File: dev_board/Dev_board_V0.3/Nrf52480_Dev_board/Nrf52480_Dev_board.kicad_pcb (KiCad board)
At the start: 4 copper layers, 72 x 75 mm, 75 parts, among them J1 Conn_01x05, J10 Conn_01x02, J11 Conn_01x05, J12 Conn_01x02, J2 USB_B_Micro, J3 SWD Debug connector, J4 Conn_01x09, J5 Conn_02x07_Top_Bottom, J6 Conn_01x07, J7 Conn_01x02, SW1 SW_Push, SW2 SW_Push, SW3 SW_Push, SW4 SW_Push, SW5 SW_Push, U1 MDBT50Q-1MV2, U3 AP2112K-3.3, U4 LIS3MDL, U5 LSM6DSOXTR, U6 SST26VF080A-104I/SN, U7 DRV2605LDGS, Y1 32.768KHz

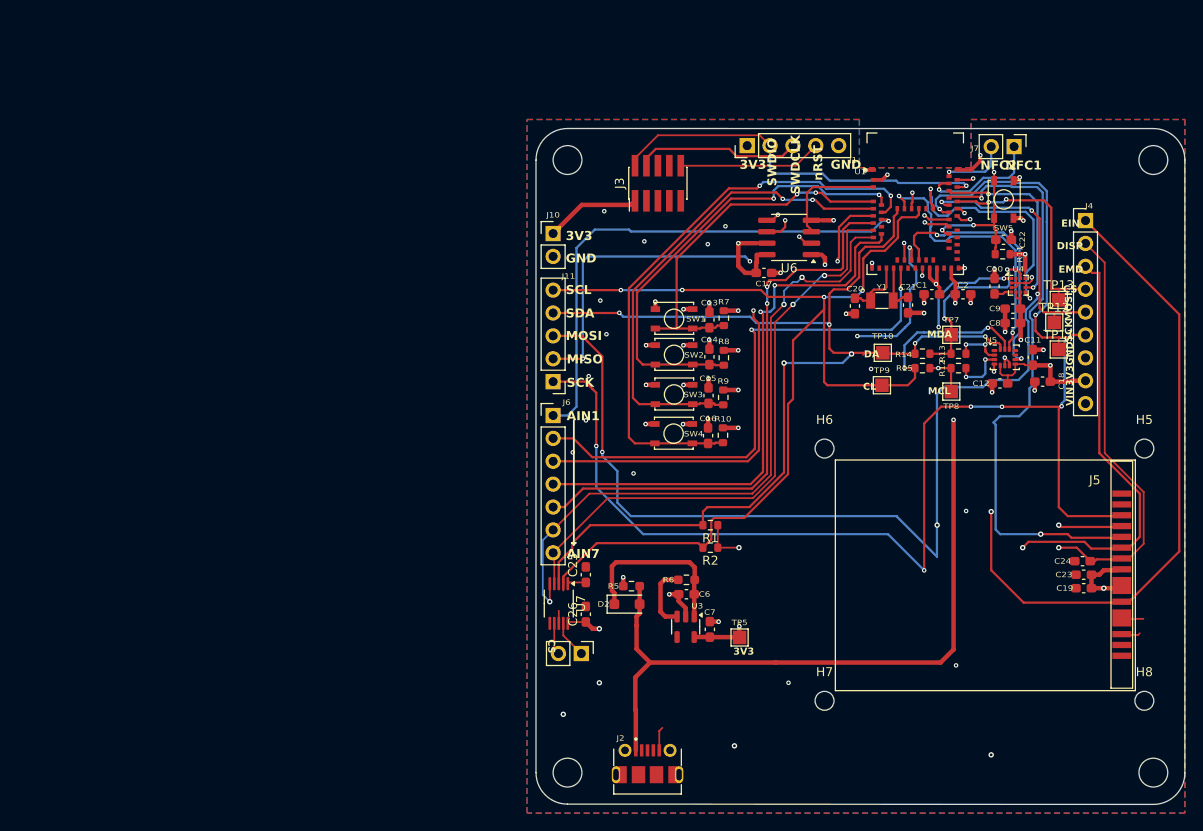
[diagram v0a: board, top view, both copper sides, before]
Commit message: lined the holes up
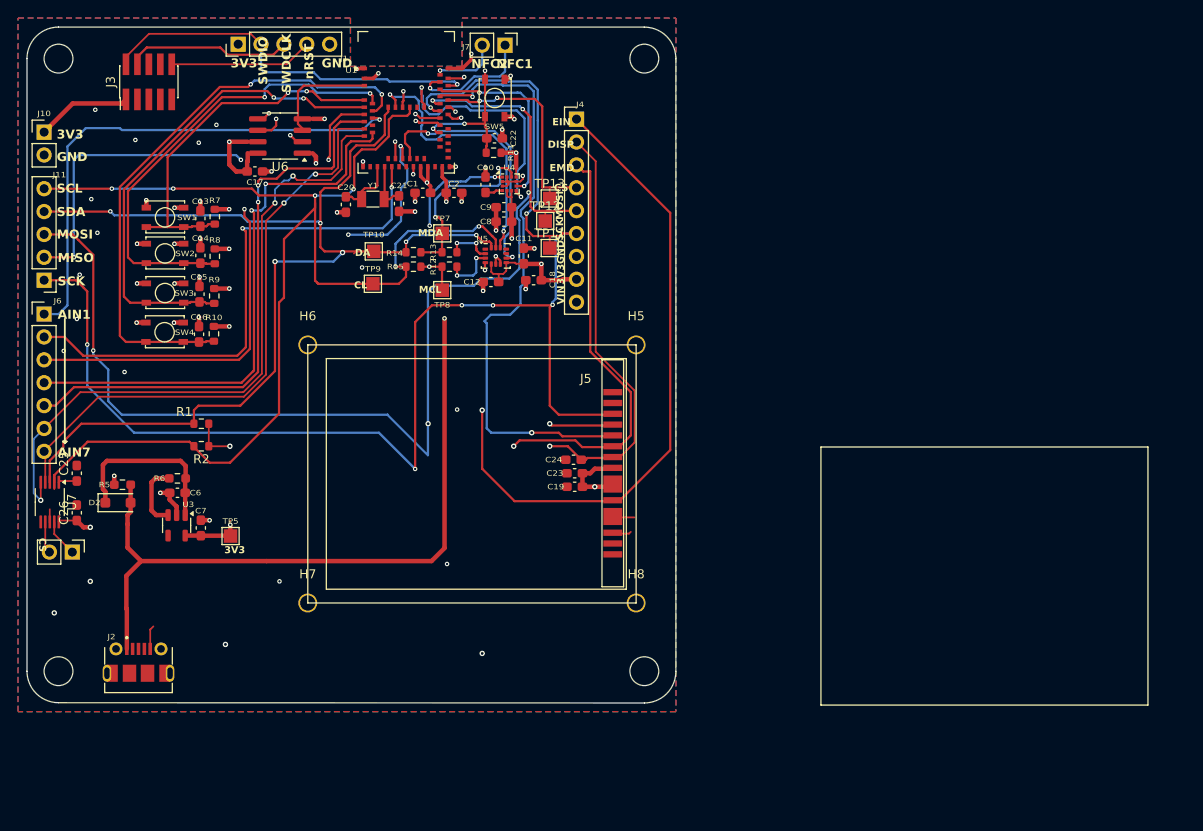
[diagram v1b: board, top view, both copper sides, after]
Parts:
- moved H6 58.5 mm to (87.1, 87.0)
- moved H7 58.4 mm to (87.1, 115.6)
- moved C10 57.6 mm to (106.9, 69.2)
- moved C11 57.6 mm to (111.1, 77.1)
- moved C15 57.6 mm to (75.1, 81.4)
- moved C17 57.6 mm to (81.3, 67.7)
- moved C18 57.6 mm to (112.2, 79.8)
- moved C19 57.6 mm to (116.8, 102.7)
- moved C2 57.6 mm to (103.4, 70.1)
- moved C20 57.6 mm to (91.4, 71.4)
- moved C21 57.6 mm to (97.3, 71.3)
- moved C22 57.6 mm to (107.9, 64.1)
- moved C23 57.6 mm to (116.8, 101.2)
- moved C7 57.6 mm to (75.3, 107.3)
- moved R11 57.6 mm to (107.8, 65.7)
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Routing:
- net /Sensors/SCL: track 140.1 -> 143.1 mm
